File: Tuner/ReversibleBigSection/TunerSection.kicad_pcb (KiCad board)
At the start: 2 copper layers, 100 x 100 mm, 121 parts, among them J1 Conn_01x03, J10 Conn_01x02, J11 Conn_02x05_Odd_Even, J12 Conn_01x01, J13 Conn_01x01, J14 Conn_01x01, J15 Conn_01x01, J16 Conn_01x01, J17 Conn_01x01, J18 Conn_01x01, J19 Conn_01x01, J2 Conn_01x03, J20 Conn_01x01, J21 Conn_01x01, J22 Conn_01x01, J23 Conn_01x02, J3 Conn_01x03, J4 Conn_01x03, J5 Conn_01x03, J6 Conn_01x03, J7 Conn_01x03, J8 Conn_01x02, J9 Conn_01x02, P10 Conn_01x01, P11 Conn_01x01, P12 Conn_01x01, P2 Conn_01x01, P3 Conn_01x01, P4 Conn_01x01, P5 Conn_01x01, P6 Conn_01x01, P7 Conn_01x01, P8 Conn_01x01, P9 Conn_01x01, U1 MCP23008, U2 ULN2803A

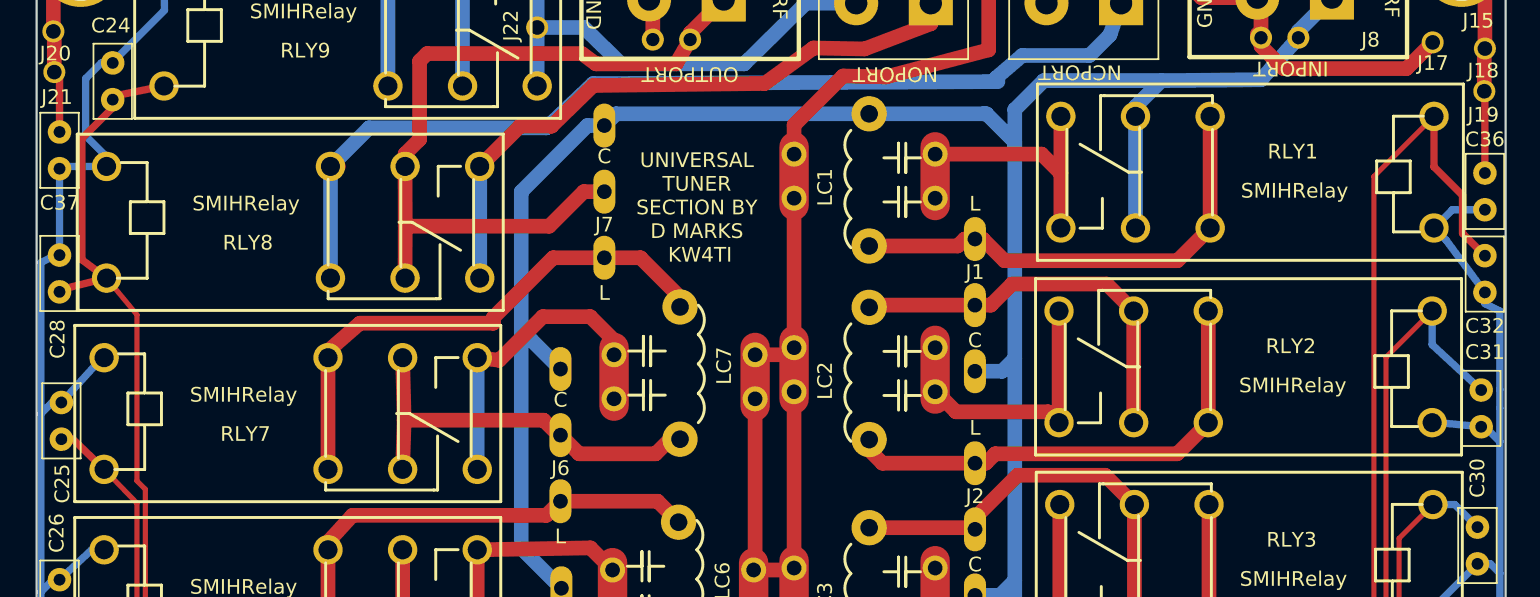
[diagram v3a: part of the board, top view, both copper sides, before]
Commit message: Added extra mounting holes to ground ReversibleLittleSection
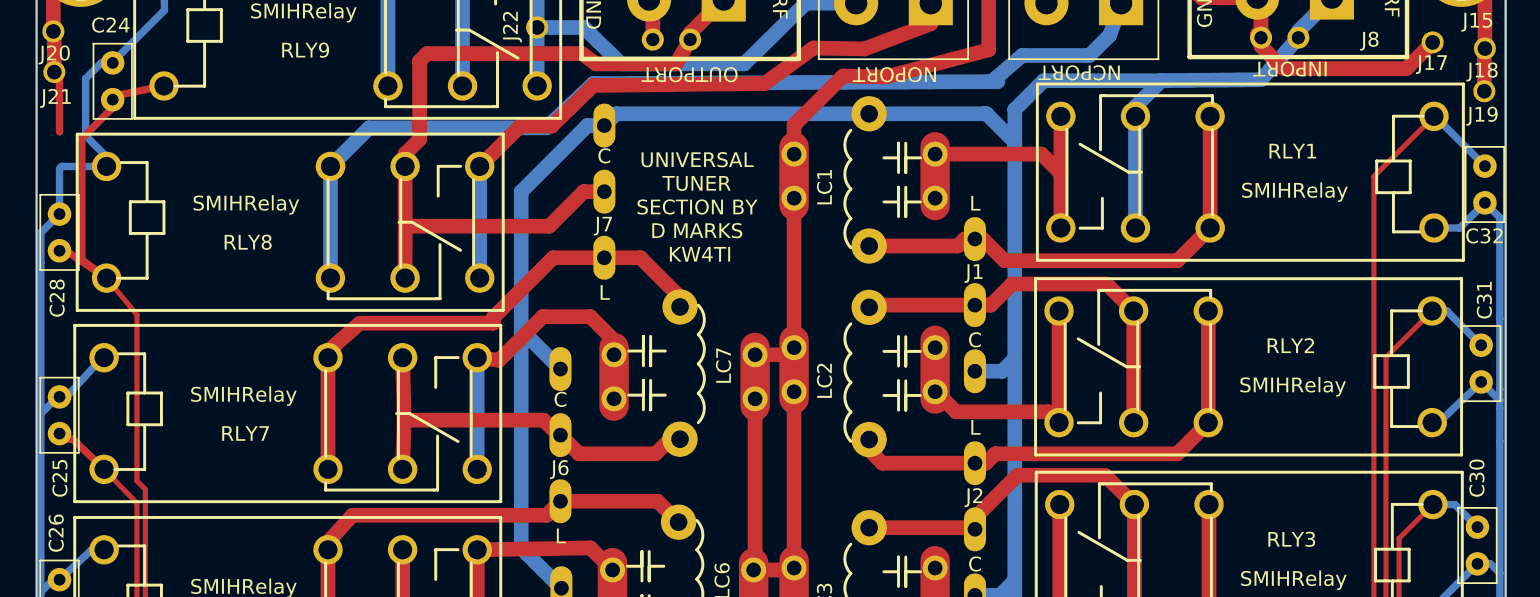
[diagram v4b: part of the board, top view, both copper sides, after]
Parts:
- removed C36, C37: 10 nF, Capacitors_THT:C_Disc_D5.0mm_W2.5mm_P2.50mm
- moved C32 6.10 mm to (148.6, 69.1)
- moved C31 3.05 mm to (148.3, 81.3)
- moved C28 2.79 mm to (51.6, 69.8)
- moved C25 0.40 mm to (51.6, 82.3)
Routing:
- net RLY1: track 127.7 -> 121.1 mm
- net Net-(J15-Pad1): track 18.2 -> 12.7 mm
- net RLY2: track 99.5 -> 97.0 mm
- net RLYPWR: track 353.9 -> 355.3 mm
- net RLY8: track 166.5 -> 167.0 mm

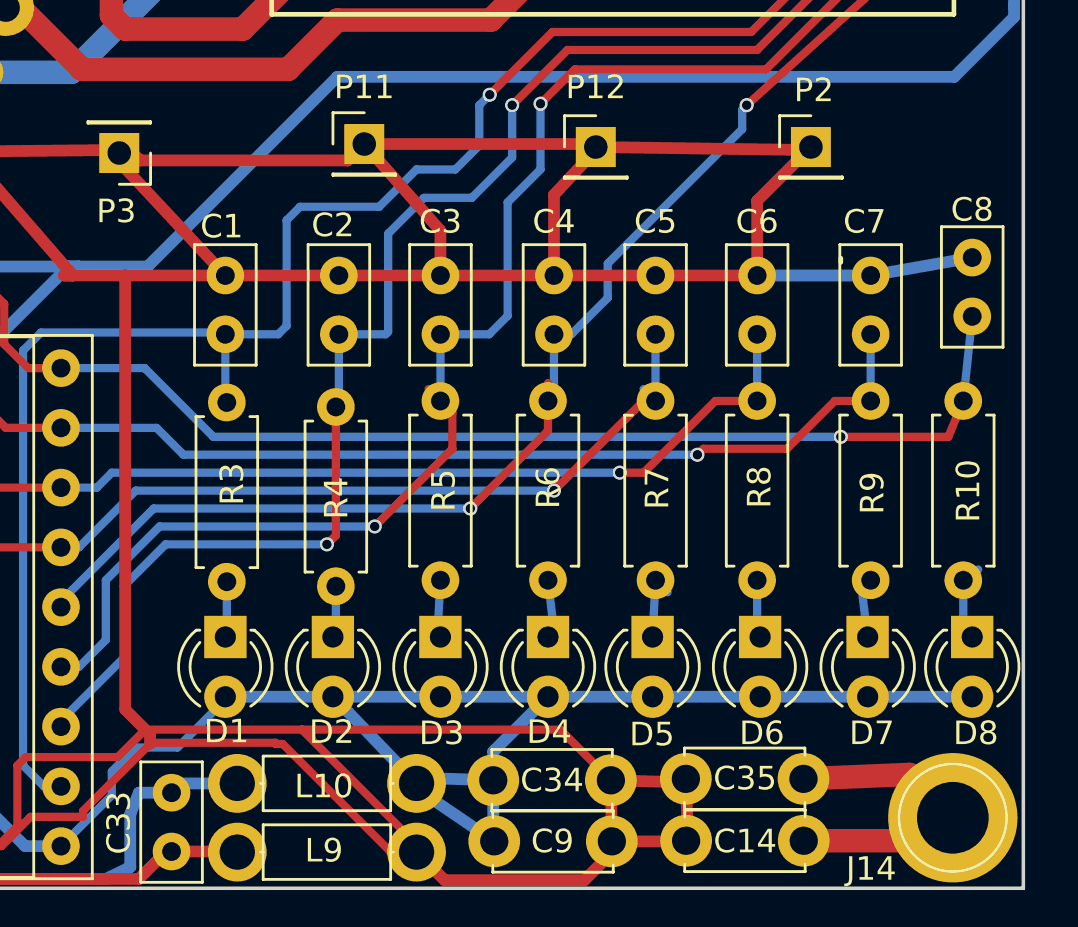
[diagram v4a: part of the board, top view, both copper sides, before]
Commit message: Added yet more ground connections
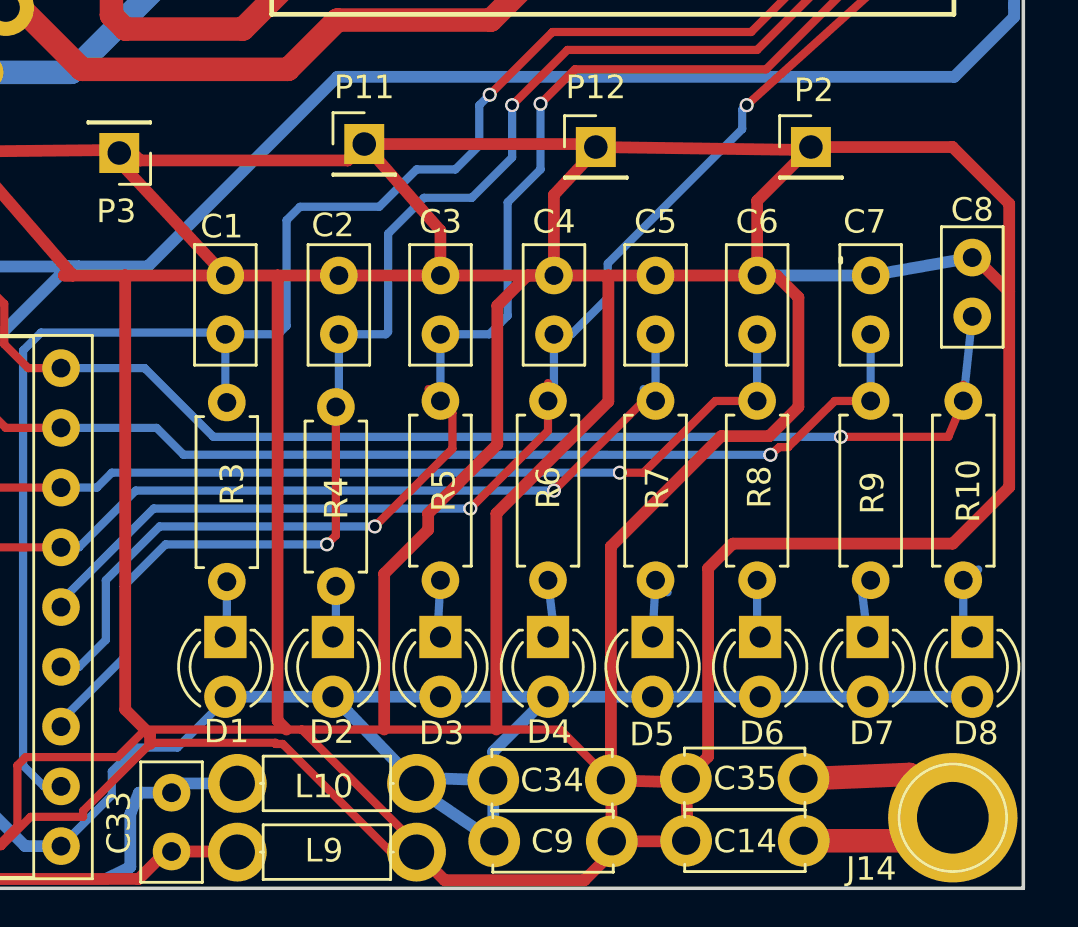
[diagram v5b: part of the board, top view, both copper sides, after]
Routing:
- net RLYGND: track 277.6 -> 415.7 mm
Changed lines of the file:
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@@
     (thickness 1.6)
     (drawings 30)
-    (tracks 1032)
+    (tracks 1067)
     (zones 0)
     (modules 119)
@@
   (segment (start 109.093 130.429) (end 113.157 130.429) (width 0.35) (layer B.Cu) (net 31) (status 10))
   (segment (start 141.986 129.286) (end 143.51 129.286) (width 0.35) (layer F.Cu) (net 31) (status 20))
-  (segment (start 139.954 131.318) (end 141.986 129.286) (width 0.35) (layer F.Cu) (net 31))
-  (segment (start 136.398 131.318) (end 139.954 131.318) (width 0.35) (layer F.Cu) (net 31))
-  (segment (start 136.144 131.572) (end 136.398 131.318) (width 0.35) (layer F.Cu) (net 31))
-  (via (at 136.144 131.572) (size 0.6) (drill 0.4) (layers F.Cu B.Cu) (net 31))
-  (segment (start 114.3 131.572) (end 136.144 131.572) (width 0.35) (layer B.Cu) (net 31))
+  (segment (start 140 131.25) (end 141.986 129.286) (width 0.35) (layer F.Cu) (net 31))
+  (segment (start 139.625 131.25) (end 140 131.25) (width 0.35) (layer F.Cu) (net 31))
+  (segment (start 139.25 131.575) (end 139.625 131.25) (width 0.35) (layer F.Cu) (net 31))
+  (via (at 139.25 131.575) (size 0.6) (drill 0.4) (layers F.Cu B.Cu) (net 31))
+  (segment (start 114.3 131.572) (end 139.25 131.575) (width 0.35) (layer B.Cu) (net 31))
   (segment (start 113.157 130.429) (end 114.3 131.572) (width 0.35) (layer B.Cu) (net 31))
   (segment (start 143.51 126.452) (end 143.51 129.286) (width 0.35) (layer B.Cu) (net 31) (status 30))
@@
   (segment (start 148.463 138.684) (end 147.828 139.319) (width 0.35) (layer B.Cu) (net 46) (status 30))
   (segment (start 147.9296 136.6012) (end 148.082 136.4488) (width 0.35) (layer B.Cu) (net 46) (status 30))
+  (segment (start 132.36 123.952) (end 132.36 129.31) (width 0.5) (layer F.Cu) (net 47))
+  (segment (start 127.6 134.07) (end 127.6 143.256) (width 0.5) (layer F.Cu) (net 47))
+  (segment (start 132.36 129.31) (end 127.6 134.07) (width 0.5) (layer F.Cu) (net 47))
+  (segment (start 147.828 123.19) (end 147.94 123.19) (width 0.5) (layer F.Cu) (net 47))
+  (segment (start 147.94 123.19) (end 149.4 124.65) (width 0.5) (layer F.Cu) (net 47))
+  (segment (start 118.3 123.952) (end 118.3 142.88) (width 0.5) (layer F.Cu) (net 47))
+  (segment (start 118.3 142.88) (end 118.676 143.256) (width 0.5) (layer F.Cu) (net 47))
+  (segment (start 130.048 123.952) (end 128.918 123.952) (width 0.5) (layer F.Cu) (net 47))
+  (segment (start 122.83 136.63) (end 122.83 143.256) (width 0.5) (layer F.Cu) (net 47))
+  (segment (start 124.7 134.76) (end 122.83 136.63) (width 0.5) (layer F.Cu) (net 47))
+  (segment (start 124.7 134.07) (end 124.7 134.76) (width 0.5) (layer F.Cu) (net 47))
+  (segment (start 127.64 131.13) (end 124.7 134.07) (width 0.5) (layer F.Cu) (net 47))
+  (segment (start 127.64 125.23) (end 127.64 131.13) (width 0.5) (layer F.Cu) (net 47))
+  (segment (start 128.918 123.952) (end 127.64 125.23) (width 0.5) (layer F.Cu) (net 47))
+  (segment (start 138.684 123.952) (end 139.512 123.952) (width 0.5) (layer F.Cu) (net 47))
+  (segment (start 132.46736 135.47264) (end 132.46736 145.40992) (width 0.5) (layer F.Cu) (net 47))
+  (segment (start 137.16 130.78) (end 132.46736 135.47264) (width 0.5) (layer F.Cu) (net 47))
+  (segment (start 139.2 130.78) (end 137.16 130.78) (width 0.5) (layer F.Cu) (net 47))
+  (segment (start 140.44 129.54) (end 139.2 130.78) (width 0.5) (layer F.Cu) (net 47))
+  (segment (start 140.44 124.88) (end 140.44 129.54) (width 0.5) (layer F.Cu) (net 47))
+  (segment (start 139.512 123.952) (end 140.44 124.88) (width 0.5) (layer F.Cu) (net 47))
+  (segment (start 140.97 118.491) (end 146.991 118.491) (width 0.5) (layer F.Cu) (net 47))
+  (segment (start 136.6 144.404) (end 135.65504 145.34896) (width 0.5) (layer F.Cu) (net 47))
+  (segment (start 136.6 136.4) (end 136.6 144.404) (width 0.5) (layer F.Cu) (net 47))
+  (segment (start 137.65 135.35) (end 136.6 136.4) (width 0.5) (layer F.Cu) (net 47))
+  (segment (start 147 135.35) (end 137.65 135.35) (width 0.5) (layer F.Cu) (net 47))
+  (segment (start 149.4 132.95) (end 147 135.35) (width 0.5) (layer F.Cu) (net 47))
+  (segment (start 149.4 120.9) (end 149.4 124.65) (width 0.5) (layer F.Cu) (net 47))
+  (segment (start 149.4 124.65) (end 149.4 132.95) (width 0.5) (layer F.Cu) (net 47))
+  (segment (start 146.991 118.491) (end 149.4 120.9) (width 0.5) (layer F.Cu) (net 47))
   (segment (start 71.8185 118.1735) (end 81.3435 118.1735) (width 0.5) (layer B.Cu) (net 47))
   (segment (start 81.3435 118.1735) (end 81.4705 118.3005) (width 0.5) (layer B.Cu) (net 47))
@@
   (segment (start 105.029 118.6815) (end 98.298 118.6815) (width 0.5) (layer F.Cu) (net 47))
   (segment (start 98.298 118.6815) (end 98.1075 118.491) (width 0.5) (layer F.Cu) (net 47))
-  (segment (start 119.3292 143.256) (end 130.31344 143.256) (width 0.35) (layer F.Cu) (net 47))
+  (segment (start 119.3292 143.256) (end 122.83 143.256) (width 0.35) (layer F.Cu) (net 47))
+  (segment (start 122.83 143.256) (end 127.6 143.256) (width 0.35) (layer F.Cu) (net 47))
+  (segment (start 127.6 143.256) (end 130.31344 143.256) (width 0.35) (layer F.Cu) (net 47))
   (segment (start 130.31344 143.256) (end 132.46736 145.40992) (width 0.35) (layer F.Cu) (net 47) (status 20))
   (segment (start 118.2116 143.8656) (end 118.5164 143.8656) (width 0.35) (layer F.Cu) (net 47))
@@
   (segment (start 118.2116 143.8148) (end 118.2116 143.8656) (width 0.35) (layer F.Cu) (net 47))
   (segment (start 101.473 148.209) (end 106.4006 148.209) (width 0.35) (layer F.Cu) (net 47) (status 10))
-  (segment (start 119.3292 143.256) (end 124.206 148.1328) (width 0.35) (layer F.Cu) (net 47) (status 20))
-  (segment (start 112.6744 143.256) (end 119.3292 143.256) (width 0.35) (layer F.Cu) (net 47))
-  (segment (start 111.506 144.4244) (end 112.6744 143.256) (width 0.35) (layer F.Cu) (net 47))
-  (segment (start 107.5944 144.4244) (end 111.506 144.4244) (width 0.35) (layer F.Cu) (net 47))
-  (segment (start 107.2388 144.78) (end 107.5944 144.4244) (width 0.35) (layer F.Cu) (net 47))
-  (segment (start 107.2388 147.3708) (end 107.2388 144.78) (width 0.35) (layer F.Cu) (net 47))
   (segment (start 106.4006 148.209) (end 107.2388 147.3708) (width 0.35) (layer F.Cu) (net 47))
+  (segment (start 107.2388 147.3708) (end 107.2388 144.78) (width 0.35) (layer F.Cu) (net 47))
+  (segment (start 107.2388 144.78) (end 107.5944 144.4244) (width 0.35) (layer F.Cu) (net 47))
+  (segment (start 107.5944 144.4244) (end 111.506 144.4244) (width 0.35) (layer F.Cu) (net 47))
+  (segment (start 111.506 144.4244) (end 112.6744 143.256) (width 0.35) (layer F.Cu) (net 47))
+  (segment (start 112.6744 143.256) (end 118.676 143.256) (width 0.35) (layer F.Cu) (net 47))
+  (segment (start 119.3292 143.256) (end 124.206 148.1328) (width 0.35) (layer F.Cu) (net 47) (status 20))
+  (segment (start 118.676 143.256) (end 119.3292 143.256) (width 0.35) (layer F.Cu) (net 47))
   (segment (start 124.206 148.1328) (end 124.206 148.463) (width 0.35) (layer F.Cu) (net 47) (status 30))
   (segment (start 135.65504 145.34896) (end 135.7414 147.9042) (width 0.5) (layer F.Cu) (net 47) (status 30))
@@
   (segment (start 143.51 123.952) (end 138.684 123.952) (width 0.5) (layer B.Cu) (net 47) (status 30))
   (segment (start 134.366 123.952) (end 138.684 123.952) (width 0.5) (layer F.Cu) (net 47) (status 30))
-  (segment (start 130.048 123.952) (end 134.366 123.952) (width 0.5) (layer F.Cu) (net 47) (status 30))
+  (segment (start 130.048 123.952) (end 132.36 123.952) (width 0.5) (layer F.Cu) (net 47) (status 30))
+  (segment (start 132.36 123.952) (end 134.366 123.952) (width 0.5) (layer F.Cu) (net 47) (status 30))
   (segment (start 125.222 123.952) (end 130.048 123.952) (width 0.5) (layer F.Cu) (net 47) (status 30))
   (segment (start 120.904 123.952) (end 125.222 123.952) (width 0.5) (layer F.Cu) (net 47) (status 30))
-  (segment (start 116.078 123.952) (end 120.904 123.952) (width 0.5) (layer F.Cu) (net 47) (status 30))
+  (segment (start 116.078 123.952) (end 118.3 123.952) (width 0.5) (layer F.Cu) (net 47) (status 30))
+  (segment (start 118.3 123.952) (end 120.904 123.952) (width 0.5) (layer F.Cu) (net 47) (status 30))
   (segment (start 116.078 123.952) (end 111.8235 123.952) (width 0.5) (layer F.Cu) (net 47) (status 10))
   (segment (start 111.8235 123.952) (end 109.22 123.952) (width 0.5) (layer F.Cu) (net 47) (status 10))
